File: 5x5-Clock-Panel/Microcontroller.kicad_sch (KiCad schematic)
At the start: 0 parts

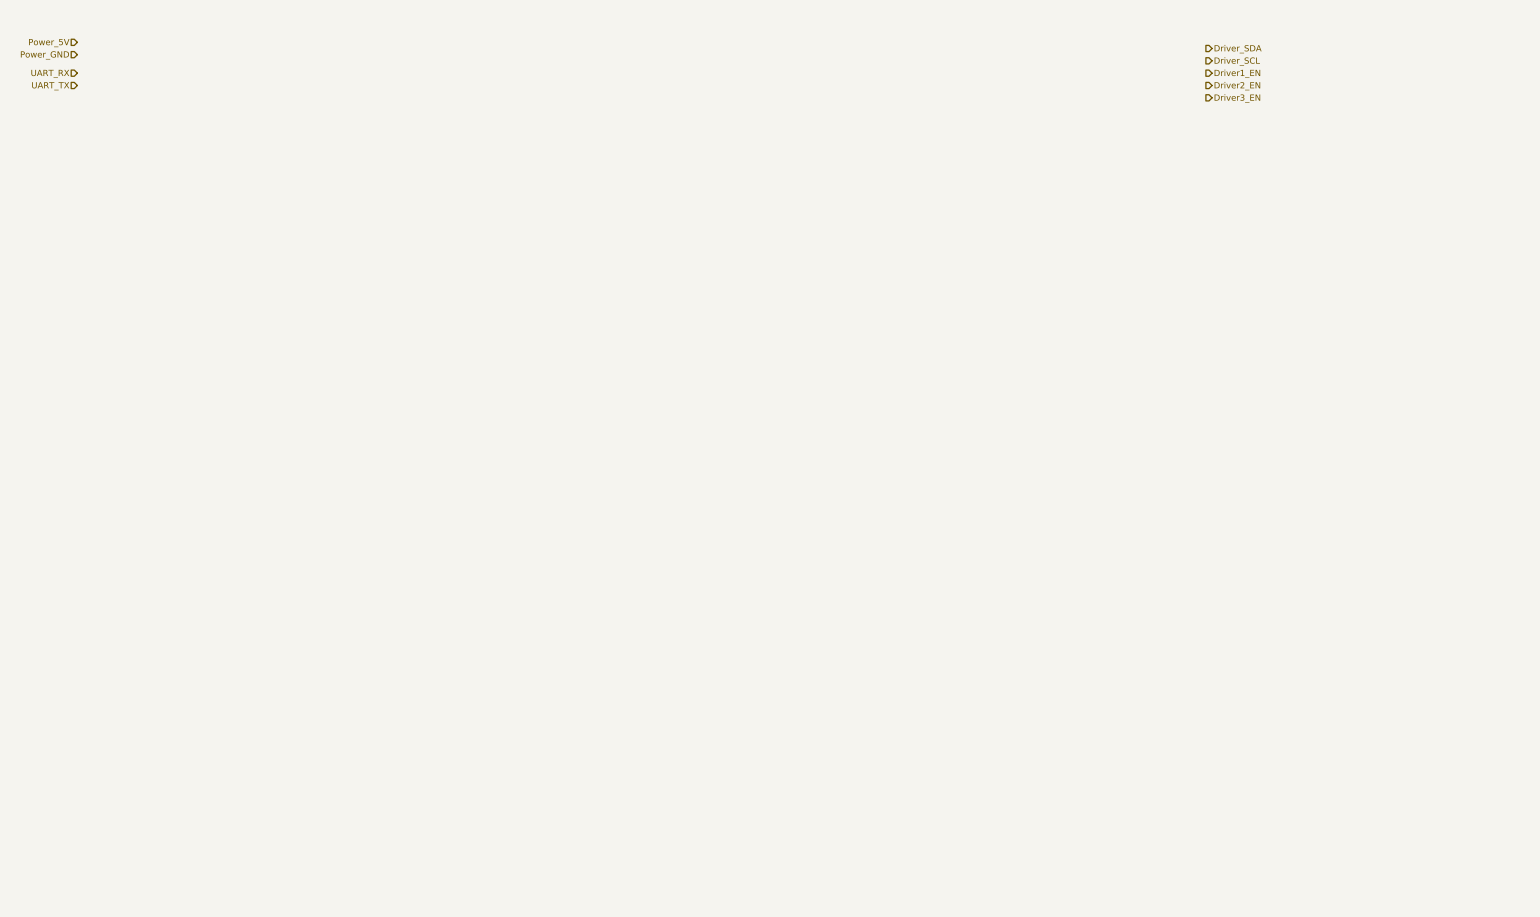
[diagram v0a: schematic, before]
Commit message: added rs485 tranceiver
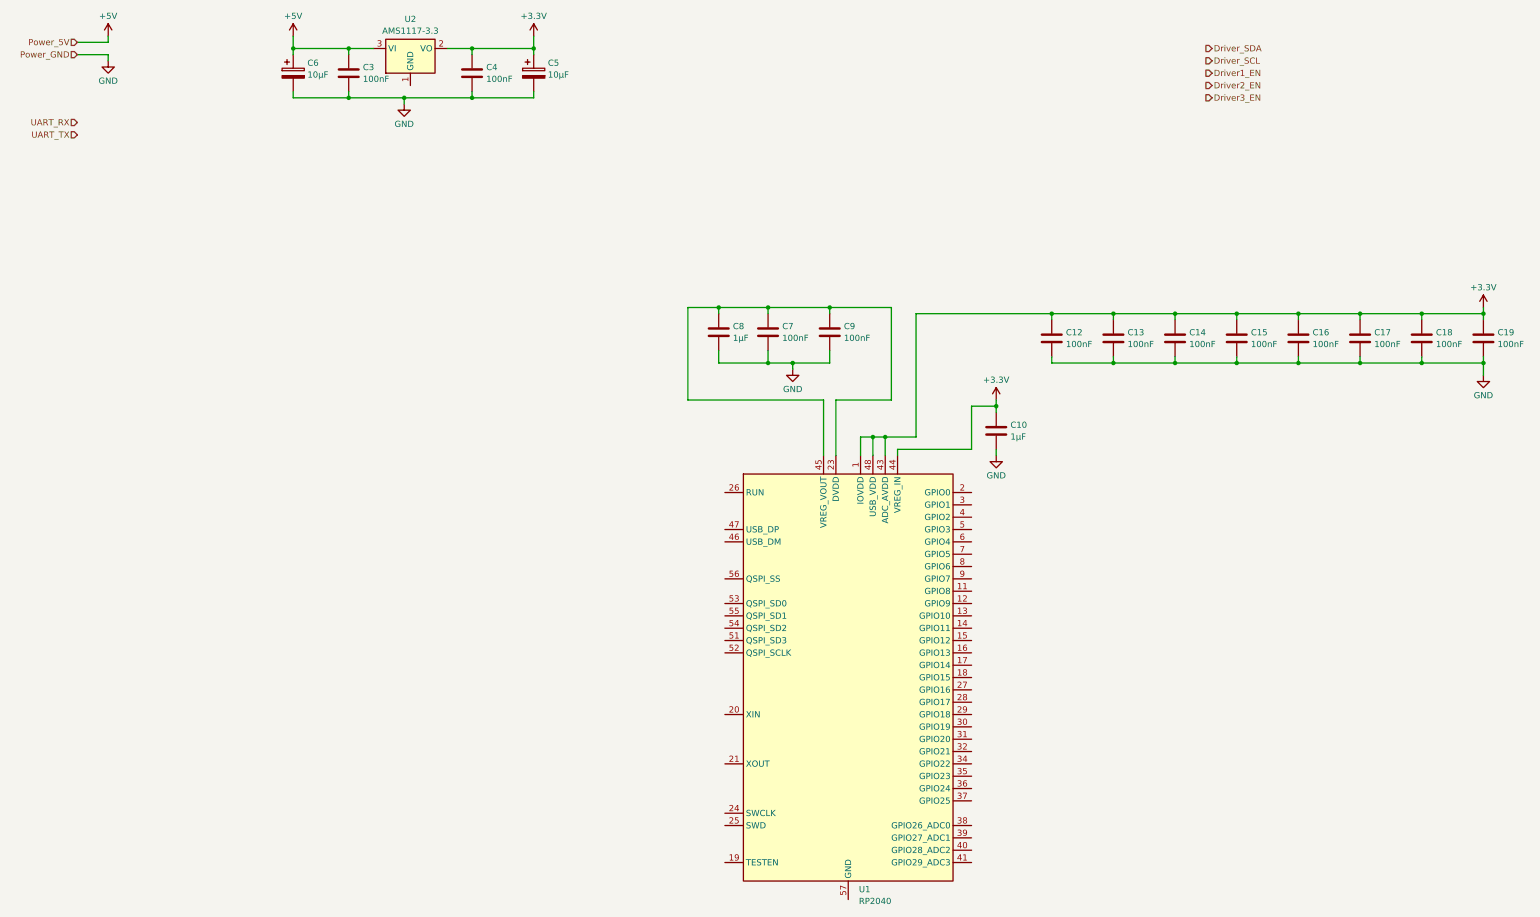
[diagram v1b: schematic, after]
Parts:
- added C10, C8: 1µF, symbol Device:C
- added C12, C13, C14, C15, C16, C17, C18, C19, C3, C4, C7, C9: 100nF, symbol Device:C
- added C5, C6: 10µF, symbol Device:C_Polarized
- added U1: RP2040, Package_DFN_QFN:QFN-56-1EP_7x7mm_P0.4mm_EP3.2x3.2mm, symbol MCU_RaspberryPi:RP2040
- added U2: AMS1117-3.3, Package_TO_SOT_SMD:SOT-223-3_TabPin2, symbol Regulator_Linear:AMS1117-3.3
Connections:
- new net: C7.1, C8.1, C9.1, U1.23 (DVDD), U1.45 (VREG_VOUT), U1.50 (DVDD)
- new net +3.3V: C10.1, C12.1, C13.1, C14.1, C15.1, C16.1, C17.1, C18.1, C19.1, C4.1, C5.1, U1.1 (IOVDD), U1.10 (IOVDD), U1.22 (IOVDD), U1.33 (IOVDD), U1.42 (IOVDD), U1.43 (ADC_AVDD), U1.44 (VREG_IN), U1.48 (USB_VDD), U1.49 (IOVDD), U2.2 (VO)
- new net +5V: C3.1, C6.1, U2.3 (VI)
- new net GND: C10.2, C12.2, C13.2, C14.2, C15.2, C16.2, C17.2, C18.2, C19.2, C3.2, C4.2, C5.2, C6.2, C7.2, C8.2, C9.2
